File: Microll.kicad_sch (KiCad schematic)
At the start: 35 parts, among them J1 Conn_01x12, J2 Conn_02x10_Top_Bottom, J3 Conn_01x08, J6 USB_C_Receptacle_USB2.0_16P, SW4 SW_DIP_x03, U1 ESP32-C3-WROOM-02-N4, U2 TLV76733DRVx, U3 STM32G0B1CBT6, U4 USBLC6-2P6, U5 DPDT_Switch_x2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

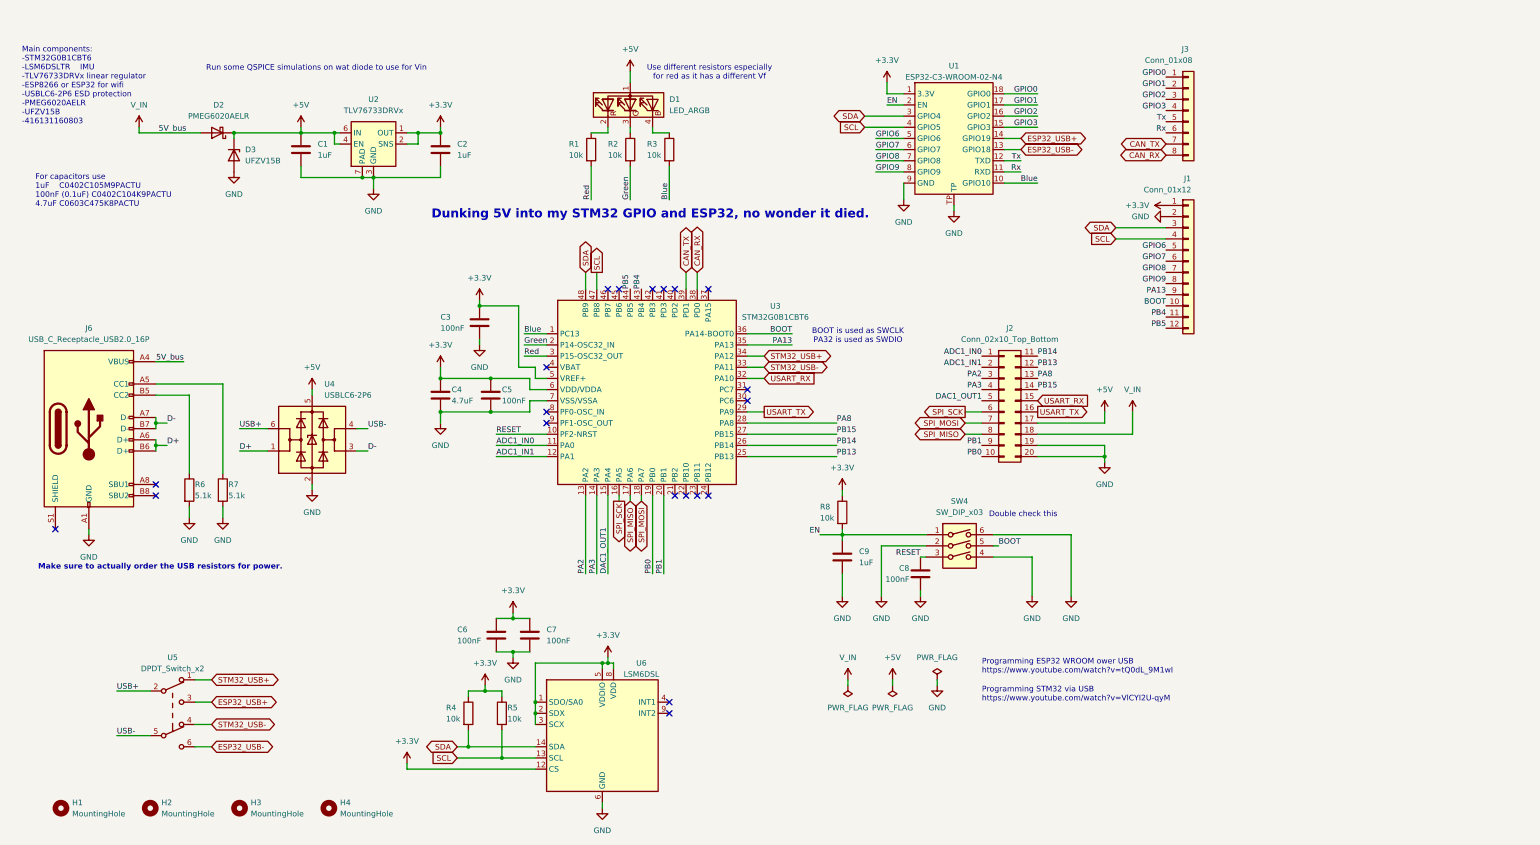
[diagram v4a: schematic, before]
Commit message: Added NMOS to control the LEDs. Changed the series resistance to set the appropriate current limit for the LEDs. Updated USB ESD protection. Added Simulations folder with LED simulation.
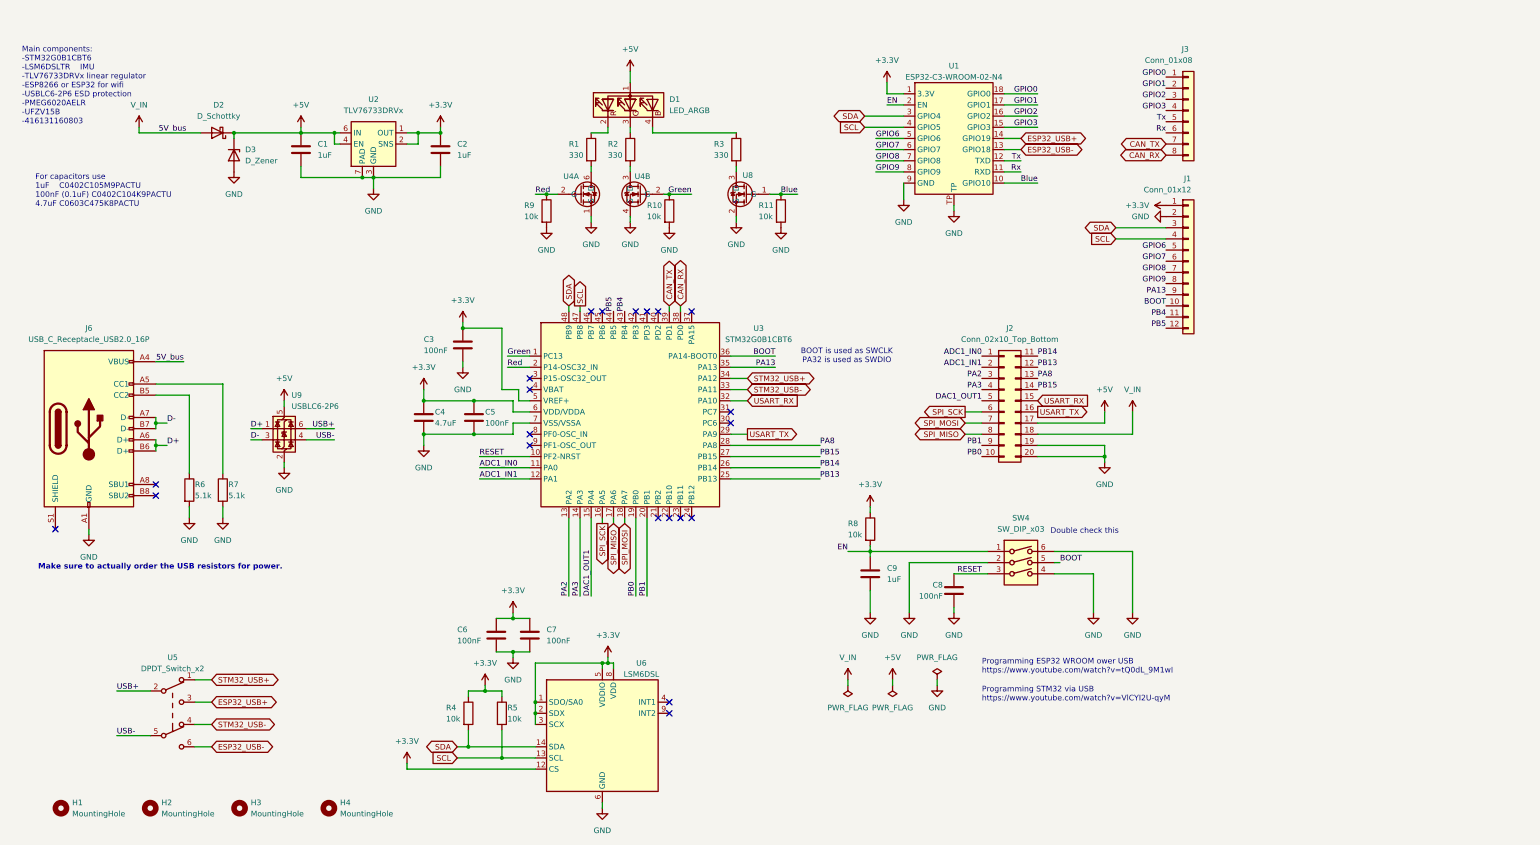
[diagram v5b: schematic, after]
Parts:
- removed U4: USBLC6-2P6, Package_TO_SOT_SMD:SOT-666, symbol Power_Protection:USBLC6-2P6
- added R10, R11, R9: 10k, Resistor_SMD:R_0402_1005Metric, symbol Device:R
- added U4: BSD235NH6327XTSA1, Package_TO_SOT_SMD:SOT-363_SC-70-6, symbol BSD235NH6327XTSA1:BSD235NH6327XTSA1
- added U8: NX7002AKW,115, Package_TO_SOT_SMD:SOT-323_SC-70, symbol NX7002AKW,115:NX7002AKW,115
- added U9: USBLC6-2P6, Package_TO_SOT_SMD:SOT-666, symbol Power_Protection:USBLC6-2P6
- D2: value PMEG6020AELR -> D_Schottky
- D3: value UFZV15B -> D_Zener
- R1, R2, R3: value 10k -> 330
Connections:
- net +5V: now also U9.5 (VBUS)
- net Blue: now also R11.1, U8.1 (G); no longer R3.2, U3.1 (PC13)
- net D+: now also U9.1 (I/O1)
- net D-: now also U9.3 (I/O2)
- net GND: now also R10.2, R11.2, R9.2, U4.1 (S), U4.4 (S), U8.2 (S), U9.2 (GND)
- net Green: now also U3.1 (PC13), R10.1, U4.2 (G); no longer R2.2, U3.2 (P14-OSC32_IN)
- net Red: now also U3.2 (P14-OSC32_IN), R9.1, U4.2 (G); no longer R1.2, U3.3 (P15-OSC32_OUT)
- net USB+: now also U9.6 (I/O1)
- net USB-: now also U9.4 (I/O2)
- new net: R3.2, U8.3 (D)
- new net: R1.2, U4.6 (D)
- new net: R2.2, U4.3 (D)
- no-connect marks 20 -> 21
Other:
- note removed: "Dunking 5V into my STM32 GPIO and ESP32, no wonder it died."
- note removed: "Run some QSPICE simulations on wat diode to use for Vin"
- note removed: "Use different resistors especially for red as it has a different Vf"
- moved on the sheet: C3, C4, C5, C8, C9, R3, R8, SW4, U3

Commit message: Updating component documentation
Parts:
- D2: value D_Schottky -> PMEG6020AELR
- D3: value D_Zener -> UFZV15B
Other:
- note added: "For resistors use 330 RC0402JR-7D330RL 5.1K 10k"
- note added: "Pontentially look for smaller alternative slide switches"
- note removed: "Make sure to actually order the USB resistors for power."
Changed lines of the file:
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@@
 	(wire
 		(pts
+			(xy 255.27 52.07) (xy 273.05 52.07)
+		)
+		(stroke
+			(width 0)
+			(type default)
+		)
+	)
+	(wire
+		(pts
 			(xy 124.46 142.24) (xy 124.46 143.51)
 		)
@@
 	(wire
 		(pts
-			(xy 261.62 54.61) (xy 273.05 54.61)
+			(xy 265.43 54.61) (xy 273.05 54.61)
 		)
 		(stroke
@@
 	(wire
 		(pts
+			(xy 255.27 49.53) (xy 273.05 49.53)
+		)
+		(stroke
+			(width 0)
+			(type default)
+		)
+	)
+	(wire
+		(pts
 			(xy 120.65 151.13) (xy 124.46 151.13)
 		)
@@
 	(wire
 		(pts
+			(xy 255.27 54.61) (xy 255.27 52.07)
+		)
+		(stroke
+			(width 0)
+			(type default)
+		)
+	)
+	(wire
+		(pts
 			(xy 214.63 130.81) (xy 232.41 130.81)
 		)
@@
 	(wire
 		(pts
-			(xy 261.62 57.15) (xy 273.05 57.15)
+			(xy 265.43 57.15) (xy 273.05 57.15)
 		)
 		(stroke
@@
 		)
 	)
-	(text "Make sure to actually order the USB resistors for power."
-		(exclude_from_sim no)
-		(at 44.196 131.826 0)
-		(effects
-			(font
-				(size 1.27 1.27)
-				(bold yes)
-			)
-		)
-	)
 	(text "Programming STM32 via USB\nhttps://www.youtube.com/watch?v=VlCYI2U-qyM"
 		(exclude_from_sim no)
@@
 		)
 	)
+	(text "For resistors use\n330 RC0402JR-7D330RL\n5.1K\n10k"
+		(exclude_from_sim no)
+		(at 16.51 62.23 0)
+		(effects
+			(font
+				(size 1.27 1.27)
+			)
+			(justify left bottom)
+		)
+	)
+	(text "Pontentially look for smaller alternative slide switches"
+		(exclude_from_sim no)
+		(at 45.974 148.59 0)
+		(effects
+			(font
+				(size 1.27 1.27)
+			)
+		)
+	)
 	(label "EN"
 		(at 200.66 128.27 180)
@@
 	(global_label "SCL"
 		(shape input)
-		(at 261.62 57.15 180)
+		(at 265.43 57.15 180)
 		(fields_autoplaced yes)
 		(effects
@@
 		)
 		(property "Intersheetrefs" "${INTERSHEET_REFS}"
-			(at 255.6993 57.0706 0)
+			(at 259.5093 57.0706 0)
 			(effects
 				(font
@@
 	(global_label "SDA"
 		(shape bidirectional)
-		(at 261.62 54.61 180)
+		(at 265.43 54.61 180)
 		(fields_autoplaced yes)
 		(effects
@@
 		)
 		(property "Intersheetrefs" "${INTERSHEET_REFS}"
-			(at 255.6388 54.6894 0)
+			(at 259.4488 54.6894 0)
 			(effects
 				(font
@@
 	(symbol
 		(lib_id "power:GND")
-		(at 273.05 52.07 270)
+		(at 255.27 54.61 0)
 		(unit 1)
 		(exclude_from_sim no)
@@
 		(fields_autoplaced yes)
 		(property "Reference" "#PWR014"
-			(at 266.7 52.07 0)
+			(at 255.27 60.96 0)
 			(effects
 				(font
@@
 		)
 		(property "Value" "GND"
-			(at 269.24 52.0699 90)
+			(at 255.27 59.69 0)
 			(effects
 				(font
 					(size 1.27 1.27)
 				)
-				(justify right)
 			)
 		)
 		(property "Footprint" ""
-			(at 273.05 52.07 0)
+			(at 255.27 54.61 0)
 			(effects
 				(font
@@
 		)
 		(property "Datasheet" ""
-			(at 273.05 52.07 0)
+			(at 255.27 54.61 0)
 			(effects
 				(font
@@
 		)
 		(property "Description" "Power symbol creates a global label with name \"GND\" , ground"
-			(at 273.05 52.07 0)
+			(at 255.27 54.61 0)
 			(effects
 				(font
@@
 			)
 		)
-		(property "Datasheet" "~"
+		(property "Datasheet" "https://www.mouser.co.uk/datasheet/2/447/PYu_RC_Group_51_RoHS_L_11-1984063.pdf"
 			(at 151.13 36.83 0)
 			(effects
@@
 			)
 		)
-		(property "Value" "D_Zener"
+		(property "Value" "UFZV15B"
 			(at 63.5 39.37 90)
 			(effects
@@
 			)
 		)
-		(property "Datasheet" "~"
+		(property "Datasheet" "https://fscdn.rohm.com/en/products/databook/datasheet/discrete/diode/zener/ufzvte-1715b-e.pdf"
 			(at 60.96 38.1 0)
 			(effects
@@
 			)
 		)
-		(property "Datasheet" "~"
+		(property "Datasheet" "https://www.mouser.co.uk/datasheet/2/447/PYu_RC_Group_51_RoHS_L_11-1984063.pdf"
 			(at 175.26 36.83 0)
 			(effects
@@
 			)
 		)
-		(property "Datasheet" "~"
+		(property "Datasheet" "https://www.mouser.co.uk/datasheet/2/447/PYu_RC_Group_51_RoHS_L_11-1984063.pdf"
 			(at 142.24 36.83 0)
 			(effects
@@
 	(symbol
 		(lib_id "power:+3.3V")
-		(at 273.05 49.53 90)
+		(at 255.27 49.53 0)
 		(unit 1)
 		(exclude_from_sim no)
@@
 		(fields_autoplaced yes)
 		(property "Reference" "#PWR012"
-			(at 276.86 49.53 0)
+			(at 255.27 53.34 0)
 			(effects
 				(font
@@
 		)
 		(property "Value" "+3.3V"
-			(at 269.24 49.5299 90)
+			(at 255.27 44.45 0)
 			(effects
 				(font
 					(size 1.27 1.27)
 				)
-				(justify left)
 			)
 		)
 		(property "Footprint" ""
-			(at 273.05 49.53 0)
+			(at 255.27 49.53 0)
 			(effects
 				(font
@@
 		)
 		(property "Datasheet" ""
-			(at 273.05 49.53 0)
+			(at 255.27 49.53 0)
 			(effects
 				(font
@@
 		)
 		(property "Description" "Power symbol creates a global label with name \"+3.3V\""
-			(at 273.05 49.53 0)
+			(at 255.27 49.53 0)
 			(effects
 				(font
@@
 			)
 		)
-		(property "Value" "D_Schottky"
+		(property "Value" "PMEG6020AELR"
 			(at 57.4675 29.21 0)
 			(effects
@@
 			)
 		)
-		(property "Datasheet" "~"
+		(property "Datasheet" "https://assets.nexperia.com/documents/data-sheet/PMEG6020AELR.pdf"
 			(at 57.15 33.02 0)
 			(effects
